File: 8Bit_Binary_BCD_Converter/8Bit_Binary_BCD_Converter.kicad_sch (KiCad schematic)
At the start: 30 parts, among them U1 74HC283, U10 74HC283, U11 74LVC2G32, U12 SN74LVC1G08DCKR, U13 74HC283, U14 74LVC2G32, U15 SN74LVC1G08DCKR, U16 74HC283, U17 74LVC2G32, U18 SN74LVC1G08DCKR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

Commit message: Finished BCD Converter + BOM + Gerber Files
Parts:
- C1, C2, C3, C4, C5, C6, C7, U2, U23: now left out of the parts list
- U1, U10, U11, U13, U14, U16, U17, U19, U20, U22, U3, U5, U7, U8: Manufacturer (none) -> Texas Instruments

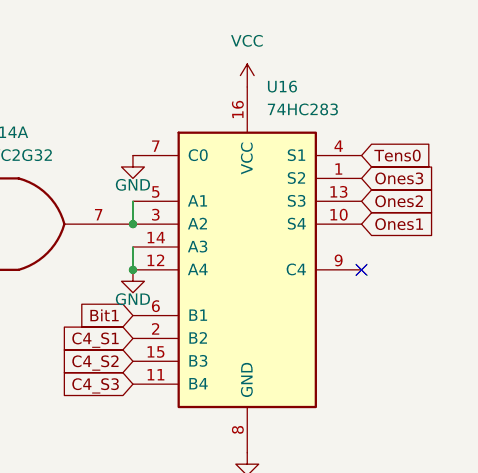
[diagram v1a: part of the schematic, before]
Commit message: BCD converter fix
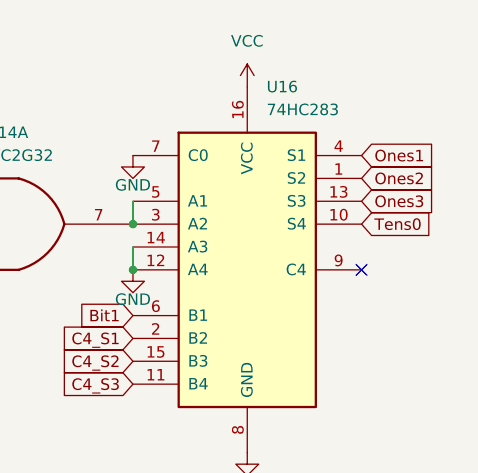
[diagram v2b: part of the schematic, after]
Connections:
- net Ones1: now also U16.4 (S1); no longer U16.10 (S4)
- net Ones2: now also U16.1 (S2); no longer U16.13 (S3)
- net Ones3: now also U16.13 (S3); no longer U16.1 (S2)
- net Tens0: now also U16.10 (S4); no longer U16.4 (S1)
